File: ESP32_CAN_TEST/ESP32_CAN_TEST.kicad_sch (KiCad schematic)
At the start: 25 parts, among them J4 Conn_01x05, SW2 EN

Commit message: update
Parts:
- removed U3: (no value), symbol Interface_CAN_LIN:SN65HVD230
- added J7: GH1.25, Connector_JST:JST_GH_BM02B-GHS-TBT_1x02-1MP_P1.25mm_Vertical, symbol Connector_Generic:Conn_01x02
- added J8: JST_2.54, Connector_JST:JST_XH_B2B-XH-AM_1x02_P2.50mm_Vertical, symbol Connector_Generic:Conn_01x02
- added Q1, Q2: 2N7002, Package_TO_SOT_SMD:SOT-23, symbol Transistor_FET:2N7002
- added R5, R6, R7, R8: 10K, Resistor_SMD:R_0805_2012Metric, symbol Device:R_Small
- added U3: TJA1050, Package_SO:SOIC-8_3.9x4.9mm_P1.27mm, symbol Interface_CAN_LIN:MCP2551-I-SN
- C1, C5: value (none) -> 22uF; footprint (none) -> Capacitor_SMD:C_0805_2012Metric
- C2, C4: value (none) -> 0.1uF; footprint (none) -> Capacitor_SMD:C_0805_2012Metric
- C3, C7: footprint (none) -> Capacitor_SMD:C_0805_2012Metric
- C6: value (none) -> 100nF; footprint (none) -> Capacitor_SMD:C_0805_2012Metric_Pad1.18x1.45mm_HandSolder
- D1: value (none) -> LED; footprint (none) -> LED_SMD:LED_0805_2012Metric_Pad1.15x1.40mm_HandSolder
- D2: value (none) -> user; footprint (none) -> LED_SMD:LED_0805_2012Metric
- J1: value (none) -> 5V in; footprint (none) -> TerminalBlock_Phoenix:TerminalBlock_Phoenix_MKDS-1,5-2_1x02_P5.00mm_Horizontal
- J2: value (none) -> Encoder_1; footprint (none) -> Connector_PinHeader_2.54mm:PinHeader_1x05_P2.54mm_Vertical
- J3: value (none) -> Molex_2x2; footprint (none) -> Connector_Molex:Molex_Micro-Fit_3.0_43045-0412_2x02_P3.00mm_Vertical
- J4: value Conn_01x05 -> Encoder2; footprint (none) -> Connector_PinHeader_2.54mm:PinHeader_1x05_P2.54mm_Vertical
- J5: value (none) -> i2C; footprint (none) -> Connector_PinSocket_2.54mm:PinSocket_1x04_P2.54mm_Vertical
- J6: value (none) -> UART; footprint (none) -> Connector_PinSocket_2.54mm:PinSocket_1x04_P2.54mm_Vertical
- JP1: value (none) -> Jumper; footprint (none) -> Jumper:SolderJumper-2_P1.3mm_Open_Pad1.0x1.5mm
- R1: value (none) -> 2K; footprint (none) -> Resistor_SMD:R_0805_2012Metric_Pad1.20x1.40mm_HandSolder
- R2: value (none) -> 10K; footprint (none) -> Resistor_SMD:R_0805_2012Metric_Pad1.20x1.40mm_HandSolder
- R3: value (none) -> 1K; footprint (none) -> Resistor_SMD:R_0805_2012Metric_Pad1.20x1.40mm_HandSolder
- R4: value (none) -> 120R; footprint (none) -> Resistor_SMD:R_0805_2012Metric_Pad1.20x1.40mm_HandSolder
- SW1: value (none) -> EN; footprint (none) -> Button_Switch_SMD:SW_SPST_TL3342
- SW2: footprint (none) -> Button_Switch_SMD:SW_SPST_TL3342
- U1: value (none) -> AMS1117; footprint (none) -> Package_TO_SOT_SMD:SOT-223-3_TabPin2
- U2: value (none) -> ESP32-WROOM-32; footprint (none) -> RF_Module:ESP32-WROOM-32
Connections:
- net +3V3: now also Q1.1 (G), Q2.1 (G), R5.1, R6.1; no longer C6.1
- net +5V: now also C6.1, J8.1 (Pin_1), R7.1, R8.1, U3.3 (VDD)
- net CANH+: now also J7.1 (Pin_1), U3.6 (CANL)
- net CANL-: now also J7.2 (Pin_2), U3.7 (CANH)
- net CAN_RX: now also Q2.2 (S), R6.2
- net CAN_TX: now also Q1.2 (S), R5.2
- net GND: now also J8.2 (Pin_2), U3.2 (VSS), U3.8 (Rs)
- net IO13: now also J2.3 (Pin_3); no longer J2.4 (Pin_4)
- net IO14: now also J2.4 (Pin_4); no longer J2.3 (Pin_3)
- new net: Q2.3 (D), R8.2, U3.4 (RXD)
- new net: Q1.3 (D), R7.2, U3.1 (TXD)
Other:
- moved on the sheet: J1, J2, J3, J4, JP1, R4

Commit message: change footprint
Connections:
- net CAN_RX: now also U2.26 (IO4); no longer U2.29 (IO5)
- net CAN_TX: now also U2.29 (IO5); no longer U2.26 (IO4)
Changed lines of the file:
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@@
     (effects (font (size 1.27 1.27)) (justify left bottom))
   )
-  (label "CAN_RX" (at 85.725 43.815 0)
+  (label "CAN_RX" (at 85.725 41.275 0)
     (effects (font (size 1.27 1.27)) (justify left bottom))
   )
@@
     (effects (font (size 1.27 1.27)) (justify left bottom))
   )
-  (label "CAN_TX" (at 85.725 41.275 0)
+  (label "CAN_TX" (at 85.725 43.815 0)
     (effects (font (size 1.27 1.27)) (justify left bottom))
   )

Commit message: powerboard mod
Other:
- moved on the sheet: C1, C2, C4, R2, SW1

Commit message: ESP,Power board update
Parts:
- removed J1: 5V in, TerminalBlock_Phoenix:TerminalBlock_Phoenix_MKDS-1,5-2_1x02_P5.00mm_Horizontal, symbol Connector:Screw_Terminal_01x02
- removed J8: JST_2.54, Connector_JST:JST_XH_B2B-XH-AM_1x02_P2.50mm_Vertical, symbol Connector_Generic:Conn_01x02
- removed U3: TJA1050, Package_SO:SOIC-8_3.9x4.9mm_P1.27mm, symbol Interface_CAN_LIN:MCP2551-I-SN
- added C10, C8, C9: (no value), symbol Device:C_Small
- added D3: (no value), symbol Device:D_TVS
- added D4, D5: (no value), symbol Device:D_Schottky
- added J1: (no value), symbol Connector_Generic:Conn_01x02
- added J8: (no value), symbol Connector:Jack-DC
- added L1: (no value), symbol Device:L_Small
- added Q3, Q4, Q5, Q6: 2N7002, Package_TO_SOT_SMD:SOT-23, symbol Transistor_FET:2N7002
- added R10, R11, R12, R13, R14, R15, R16, R17, R18, R19, R9: 10K, Resistor_SMD:R_0805_2012Metric, symbol Device:R_Small
- added U3: (no value), symbol Regulator_Switching:AOZ1282CI
- added U4: (no value), symbol Interface_CAN_LIN:SN65HVD230
- C6: value 100nF -> (none); footprint Capacitor_SMD:C_0805_2012Metric_Pad1.18x1.45mm_HandSolder -> (none)
- R5, R6, R7: value 10K -> (none); footprint Resistor_SMD:R_0805_2012Metric -> (none)
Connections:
- net +3V3: now also R8.1, C10.2, Q3.1 (G), Q4.1 (G), Q5.1 (G), Q6.1 (G), R10.1, R14.1, R15.1, R16.1, R9.1, U4.3 (VCC); no longer R5.1, R6.1
- net +5V: now also R7.2, C9.1, J8.1, L1.2, R11.1, R12.1, R13.1, R17.1, R18.1, R19.1; no longer C6.1, R7.1, R8.1
- net CANH+: now also J7.2 (Pin_2), U4.6 (CANL); no longer J7.1 (Pin_1)
- net CANL-: now also J7.1 (Pin_1), U4.7 (CANH); no longer J7.2 (Pin_2)
- net CAN_RX: now also U4.4 (R); no longer Q2.2 (S), R6.2
- net CAN_TX: now also U4.1 (D); no longer Q1.2 (S), R5.2
- net GND: now also R6.2, C10.1, C9.2, D3.1 (A1), D5.2 (A), J1.1 (Pin_1), J8.2, U3.2 (GND), U4.2 (GND), U4.8 (Rs)
- net IO13: now also Q2.2 (S), R9.2; no longer J2.3 (Pin_3)
- net IO14: now also Q3.2 (S), R10.2; no longer J2.4 (Pin_4)
- net IO15: now also Q1.2 (S), R8.2; no longer J2.2 (Pin_2)
- net IO16: now also Q6.2 (S), R16.2; no longer J4.4 (Pin_4)
- net IO17: now also Q5.2 (S), R15.2; no longer J4.3 (Pin_3)
- net IO18: now also Q4.2 (S), R14.2; no longer J4.2 (Pin_2)
- net at Q2.3 (D): now also J2.3 (Pin_3), R12.2; no longer R8.2
- net at Q1.3 (D): now also J2.2 (Pin_2), R11.2; no longer R7.2
- new net: C8.1, U3.1 (BST)
- new net: R6.1, R7.1, U3.3 (FB)
- new net: R5.2, U3.4 (EN)
- new net: C6.1, D4.1 (K), R5.1, U3.5 (VIN)
- new net: C8.2, D5.1 (K), L1.1, U3.6 (LX)
- new net: J4.2 (Pin_2), Q4.3 (D), R17.2
- new net: J4.4 (Pin_4), Q6.3 (D), R19.2
- new net: J4.3 (Pin_3), Q5.3 (D), R18.2
- new net: J2.4 (Pin_4), Q3.3 (D), R13.2
- new net +24V: D3.2 (A2), D4.2 (A), J1.2 (Pin_2)
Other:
- note added: "24v to 5v convertor"
- note added: "5v to 3.3v LDO"
- moved on the sheet: J2, J4, J5, J6

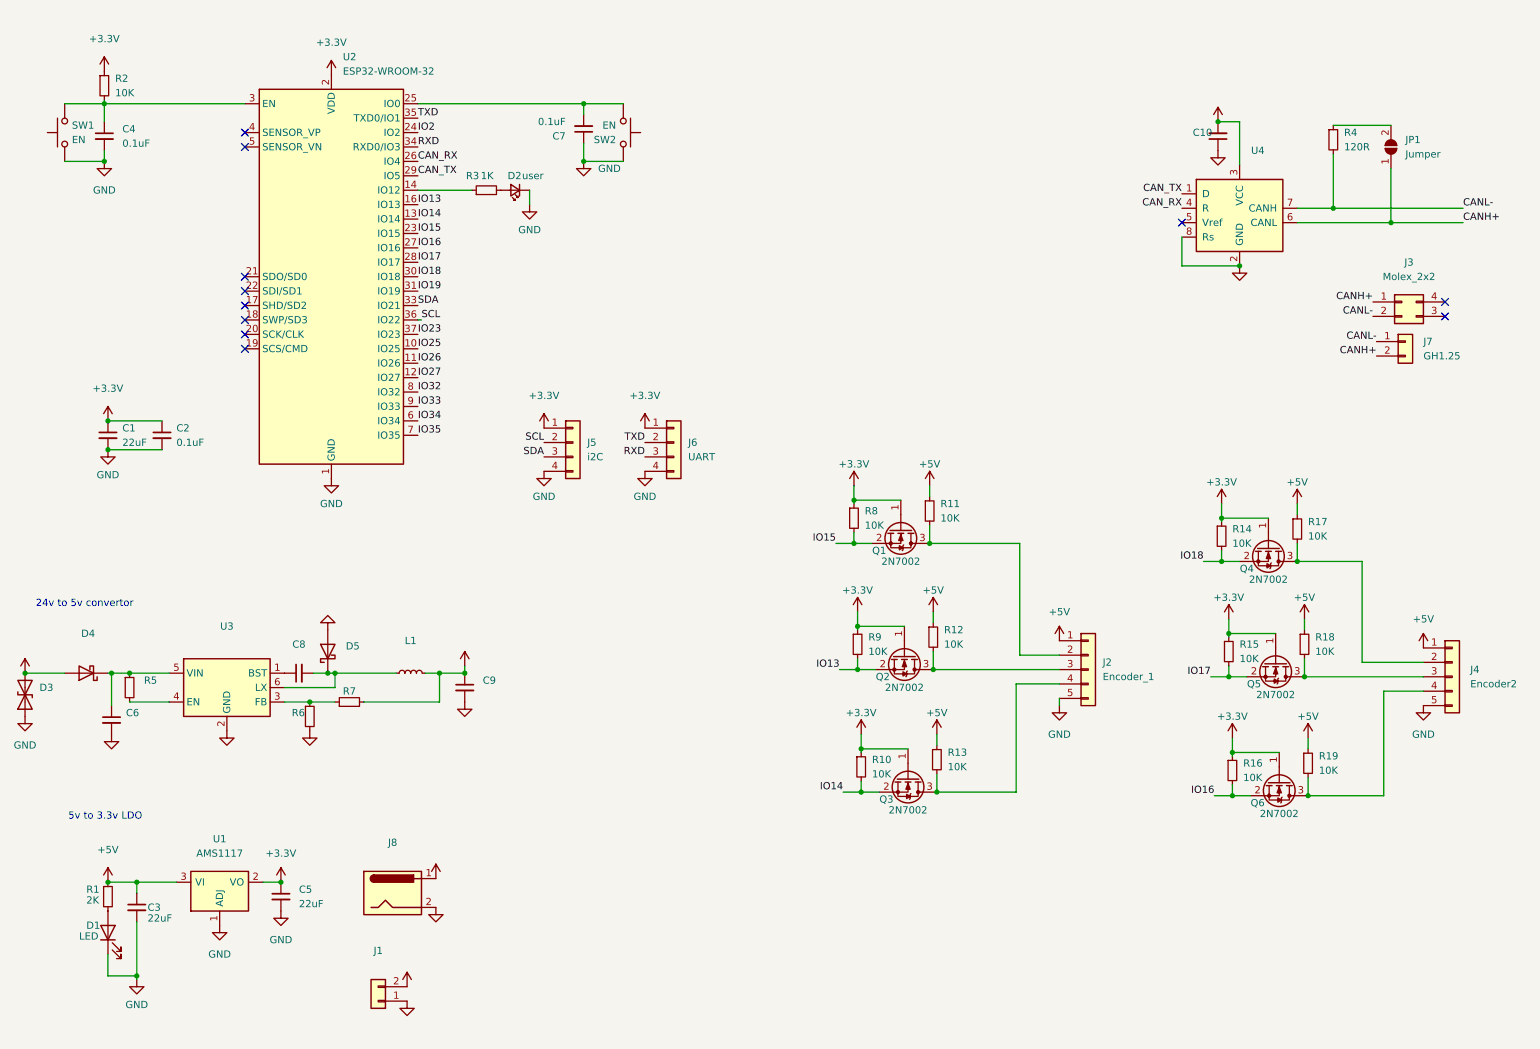
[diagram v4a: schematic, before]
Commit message: esp32 fixed canbus
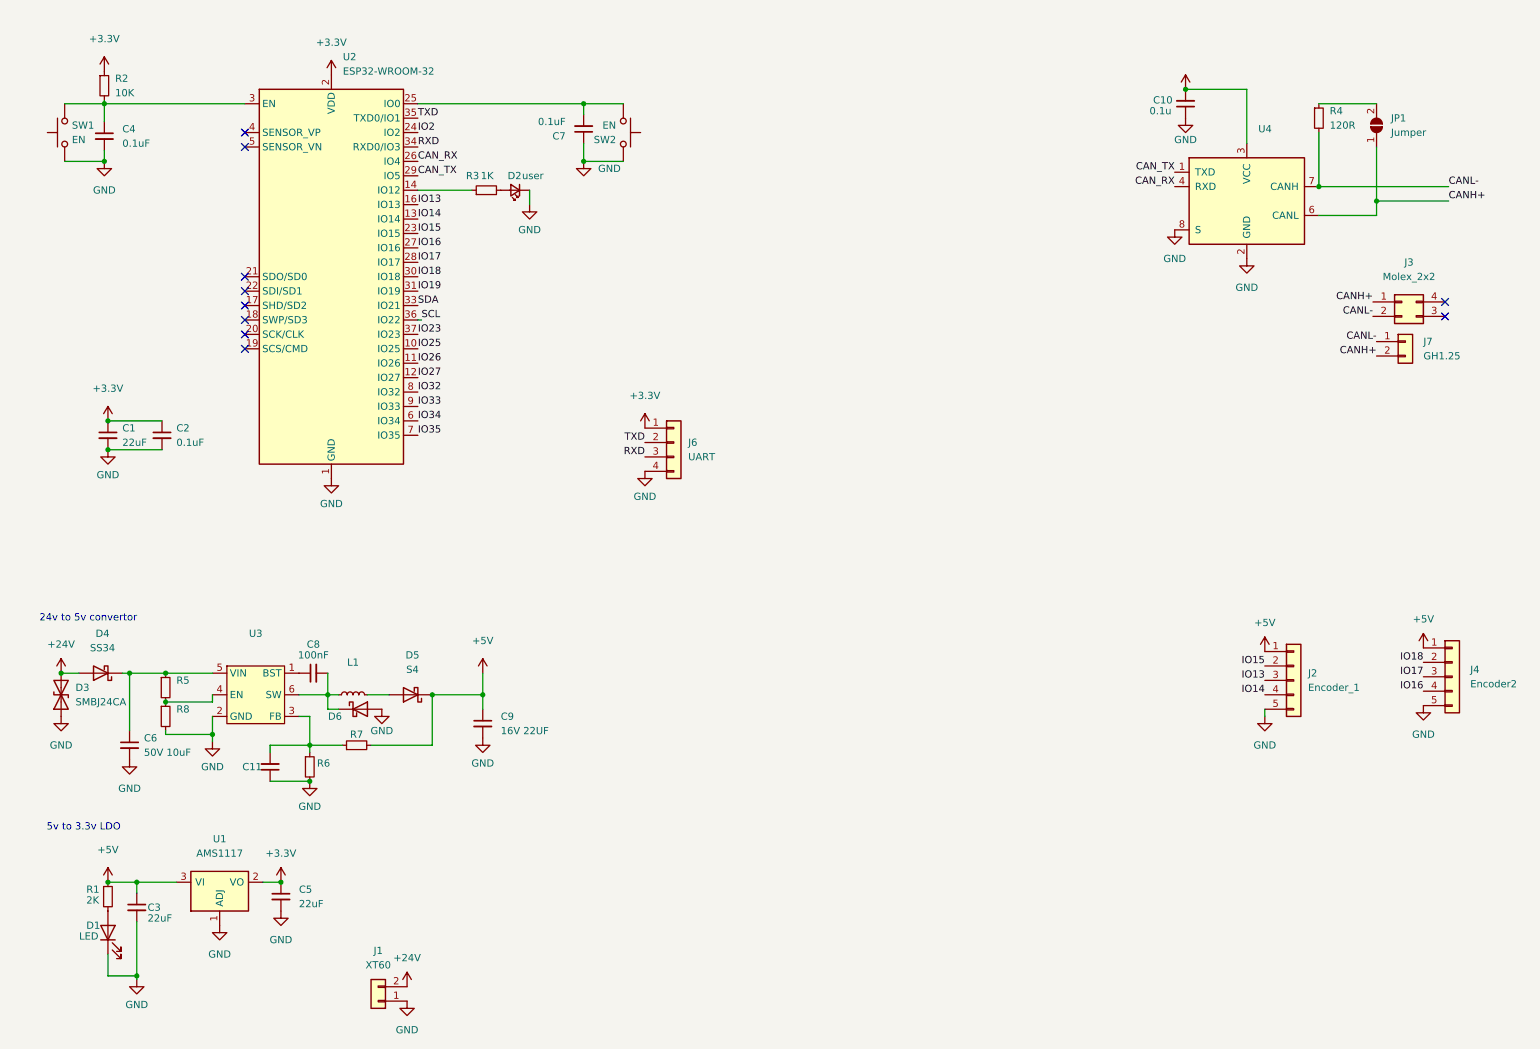
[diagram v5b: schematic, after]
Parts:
- removed J5: i2C, Connector_PinSocket_2.54mm:PinSocket_1x04_P2.54mm_Vertical, symbol Connector_Generic:Conn_01x04
- removed J8: (no value), symbol Connector:Jack-DC
- removed Q1, Q2, Q3, Q4, Q5, Q6: 2N7002, Package_TO_SOT_SMD:SOT-23, symbol Transistor_FET:2N7002
- removed R10, R11, R12, R13, R14, R15, R16, R17, R18, R19, R9: 10K, Resistor_SMD:R_0805_2012Metric, symbol Device:R_Small
- removed U3: (no value), symbol Regulator_Switching:AOZ1282CI
- removed U4: (no value), symbol Interface_CAN_LIN:SN65HVD230
- added C11: (no value), Capacitor_SMD:C_0805_2012Metric, symbol Device:C_Small
- added D6: (no value), symbol Device:D_Schottky
- added U3: (no value), symbol PolyuRobotics:MP2451
- added U4: (no value), symbol Interface_CAN_LIN:TJA1051T
- C10: value (none) -> 0.1u; footprint (none) -> Capacitor_SMD:C_0805_2012Metric
- C6: value (none) -> 50V 10uF; footprint (none) -> Capacitor_SMD:CP_Elec_6.3x7.7
- C8: value (none) -> 100nF; footprint (none) -> Capacitor_SMD:C_0805_2012Metric
- C9: value (none) -> 16V 22UF; footprint (none) -> Capacitor_SMD:CP_Elec_6.3x7.7
- D3: value (none) -> SMBJ24CA; footprint (none) -> Diode_SMD:D_SMB
- D4: value (none) -> SS34; footprint (none) -> Diode_SMD:D_SMB
- D5: value (none) -> S4; footprint (none) -> Diode_SMD:D_SOD-323F
- J1: value (none) -> XT60; footprint (none) -> Connector_AMASS:AMASS_XT60-M_1x02_P7.20mm_Vertical
- L1: footprint (none) -> Inductor_SMD:L_Vishay_IHLP-1616
- R5, R6, R7: footprint (none) -> Resistor_SMD:R_0805_2012Metric
- R8: value 10K -> (none)
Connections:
- net +3V3: no longer C10.2, R8.1
- net +5V: now also C10.2, D5.1 (K), U4.3 (VCC); no longer L1.2
- net CANH+: now also U4.6 (CANL)
- net CANL-: now also U4.7 (CANH)
- net CAN_RX: now also U4.4 (RXD)
- net CAN_TX: now also U4.1 (TXD)
- net GND: now also R8.2, C11.1, D6.2 (A), U3.2 (GND), U4.2 (GND), U4.8 (S); no longer D5.2 (A)
- net IO13: now also J2.3 (Pin_3)
- net IO14: now also J2.4 (Pin_4)
- net IO15: now also J2.2 (Pin_2); no longer R8.2
- net IO16: now also J4.4 (Pin_4)
- net IO17: now also J4.3 (Pin_3)
- net IO18: now also J4.2 (Pin_2)
- net at C8.1: now also U3.1 (BST)
- net at R6.1, R7.1: now also C11.2, U3.3 (FB)
- net at R5.2: now also R8.1, U3.4 (EN)
- net at C6.1, D4.1 (K), R5.1: now also U3.5 (VIN)
- net at C8.2, L1.1: now also D6.1 (K), U3.6 (SW); no longer D5.1 (K)
- new net: D5.2 (A), L1.2
- no-connect marks 11 -> 10
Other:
- moved on the sheet: C10, C6, C8, C9, D3, D4, J2, JP1, L1, R4, R5, R6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

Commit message: esp32 fixed canbus
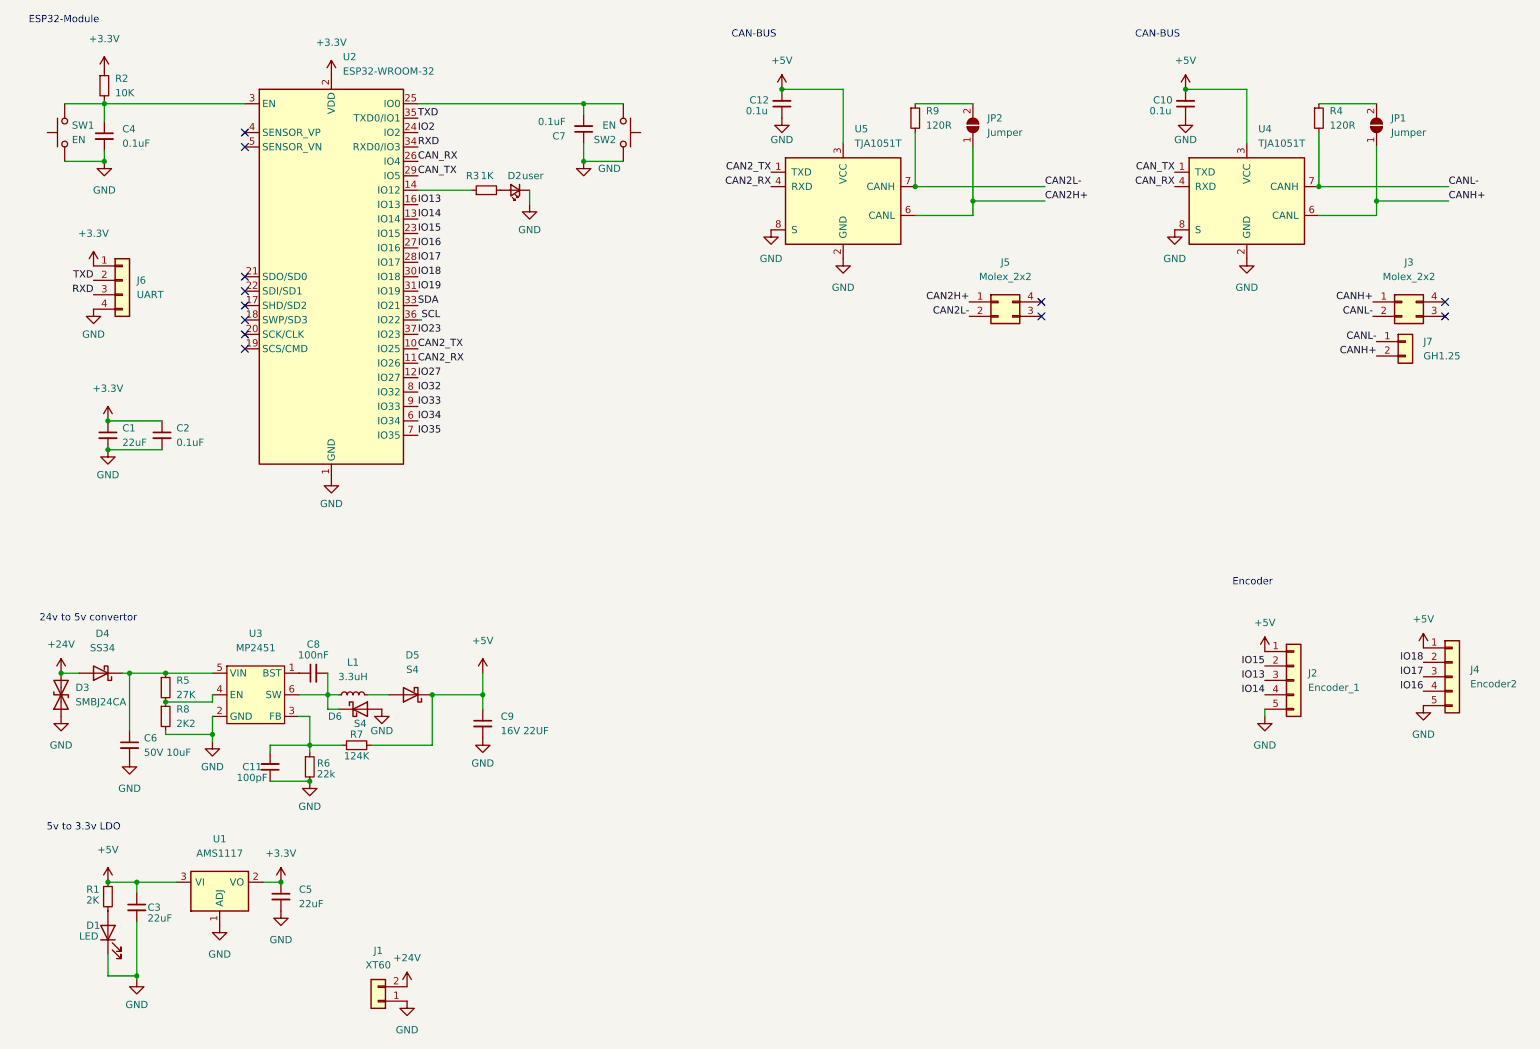
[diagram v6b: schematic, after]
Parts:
- added C12: 0.1u, Capacitor_SMD:C_0805_2012Metric, symbol Device:C_Small
- added J5: Molex_2x2, Connector_Molex:Molex_Micro-Fit_3.0_43045-0412_2x02_P3.00mm_Vertical, symbol Connector_Generic:Conn_02x02_Counter_Clockwise
- added JP2: Jumper, Jumper:SolderJumper-2_P1.3mm_Open_Pad1.0x1.5mm, symbol Jumper:SolderJumper_2_Open
- added R9: 120R, Resistor_SMD:R_0805_2012Metric_Pad1.20x1.40mm_HandSolder, symbol Device:R_Small
- added U5: TJA1051T, Package_SO:SOIC-8_3.9x4.9mm_P1.27mm, symbol Interface_CAN_LIN:TJA1051T
- C11: value (none) -> 100pF
- D6: value (none) -> S4; footprint (none) -> Diode_SMD:D_SOD-323F
- L1: value (none) -> 3.3uH
- R5: value (none) -> 27K
- R6: value (none) -> 22k
- R7: value (none) -> 124K
- R8: value (none) -> 2K2
- U3: value (none) -> MP2451; footprint (none) -> Package_TO_SOT_SMD:SOT-23-6_Handsoldering
- U4: value (none) -> TJA1051T; footprint (none) -> Package_SO:SOIC-8_3.9x4.9mm_P1.27mm
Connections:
- net +5V: now also C12.2, U5.3 (VCC)
- net GND: now also C12.1, U5.2 (GND), U5.8 (S)
- net IO25 renamed CAN2_TX
- net CAN2_TX: now also U5.1 (TXD)
- net IO26 renamed CAN2_RX
- net CAN2_RX: now also U5.4 (RXD)
- new net: JP2.2 (B), R9.1
- new net CAN2H+: J5.1 (Pin_1), JP2.1 (A), U5.6 (CANL)
- new net CAN2L-: J5.2 (Pin_2), R9.2, U5.7 (CANH)
- no-connect marks 10 -> 12
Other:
- note added: "CAN-BUS"
- note added: "ESP32-Module"
- note added: "Encoder"
- moved on the sheet: J6

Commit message: sad
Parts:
- removed C11: 100pF, Capacitor_SMD:C_0805_2012Metric, symbol Device:C_Small
- removed C8: 100nF, Capacitor_SMD:C_0805_2012Metric, symbol Device:C_Small
- removed D5, D6: S4, Diode_SMD:D_SOD-323F, symbol Device:D_Schottky
- removed L1: 3.3uH, Inductor_SMD:L_Vishay_IHLP-1616, symbol Device:L_Small
- removed R5: 27K, Resistor_SMD:R_0805_2012Metric, symbol Device:R_Small
- removed R6: 22k, Resistor_SMD:R_0805_2012Metric, symbol Device:R_Small
- removed R7: 124K, Resistor_SMD:R_0805_2012Metric, symbol Device:R_Small
- removed R8: 2K2, Resistor_SMD:R_0805_2012Metric, symbol Device:R_Small
- removed U3: MP2451, Package_TO_SOT_SMD:SOT-23-6_Handsoldering, symbol PolyuRobotics:MP2451
- added U3: (no value), symbol PolyuRobotics:MP1584
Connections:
- net +5V: now also U3.OUT2+ (VOUT+)
- net GND: now also U3.IN2- (VIN-), U3.OUT2- (VOUT-)
- net at C6.1, D4.1 (K): now also U3.IN2+ (VIN+)
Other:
- moved on the sheet: C6, C9

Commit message: new esp
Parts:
- J1: footprint Connector_AMASS:AMASS_XT60-M_1x02_P7.20mm_Vertical -> (none)
- U3: value (none) -> MP1584; footprint (none) -> PolyuRobotics:DC-DC-mp1584_module
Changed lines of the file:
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@@
     (property "Reference" "J1" (id 0) (at 78.74 180.34 0))
     (property "Value" "XT60" (id 1) (at 78.74 182.88 0))
-    (property "Footprint" "Connector_AMASS:AMASS_XT60-M_1x02_P7.20mm_Vertical" (id 2) (at 78.74 189.23 0)
+    (property "Footprint" "" (id 2) (at 78.74 189.23 0)
       (effects (font (size 1.27 1.27)) hide)
     )
@@
       (effects (font (size 1.27 1.27)) (justify left bottom) hide)
     )
-    (property "Value" "" (id 1) (at 46.99 141.605 0)
+    (property "Value" "MP1584" (id 1) (at 46.99 141.605 0)
       (effects (font (size 1.27 1.27)) (justify left bottom) hide)
     )
-    (property "Footprint" "" (id 2) (at 55.88 141.605 0)
+    (property "Footprint" "PolyuRobotics:DC-DC-mp1584_module" (id 2) (at 55.88 141.605 0)
       (effects (font (size 1.27 1.27)) (justify left bottom) hide)
     )
@@
     )
     (path "/4fb4bdaf-e38c-4dd4-83fa-42c415efbf1f"
-      (reference "J1") (unit 1) (value "XT60") (footprint "Connector_AMASS:AMASS_XT60-M_1x02_P7.20mm_Vertical")
+      (reference "J1") (unit 1) (value "XT60") (footprint "Connector_AMASS:AMASS_XT30U-M_1x02_P5.0mm_Vertical")
     )
     (path "/47b86a97-732d-47d4-9b24-328bd9592eaa"
